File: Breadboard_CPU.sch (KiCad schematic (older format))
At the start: 21 parts, among them Q101 2N2222, SW101 RST

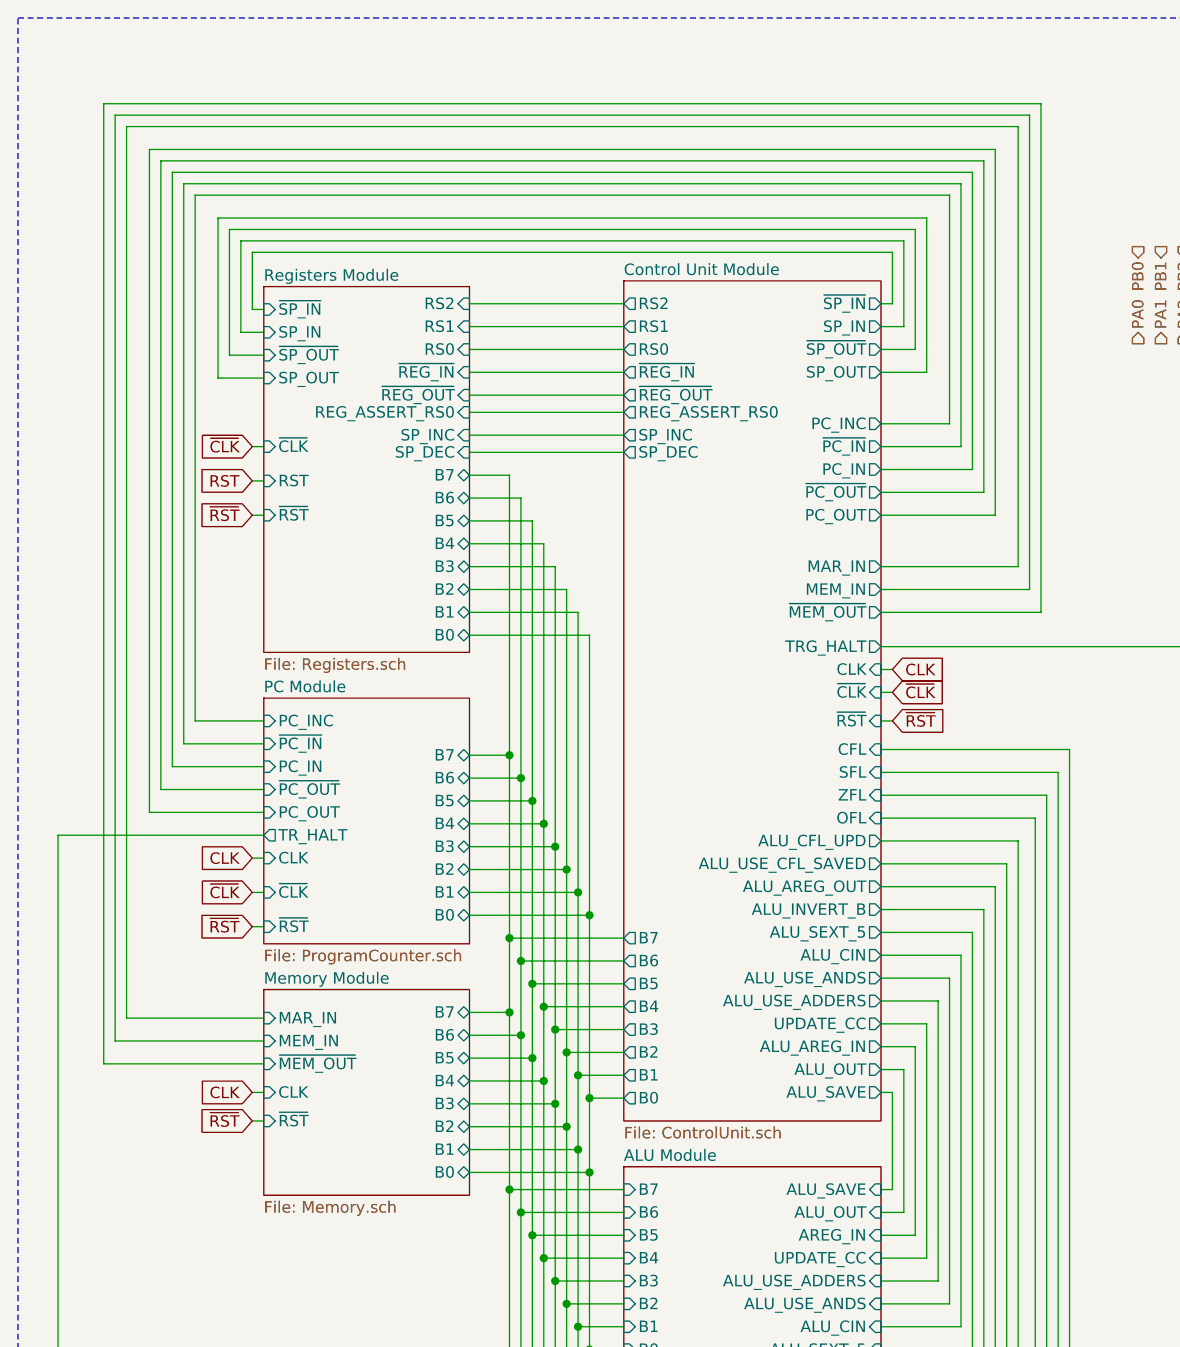
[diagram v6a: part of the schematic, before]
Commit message: Pre-removal of H/L byte deciding hardware
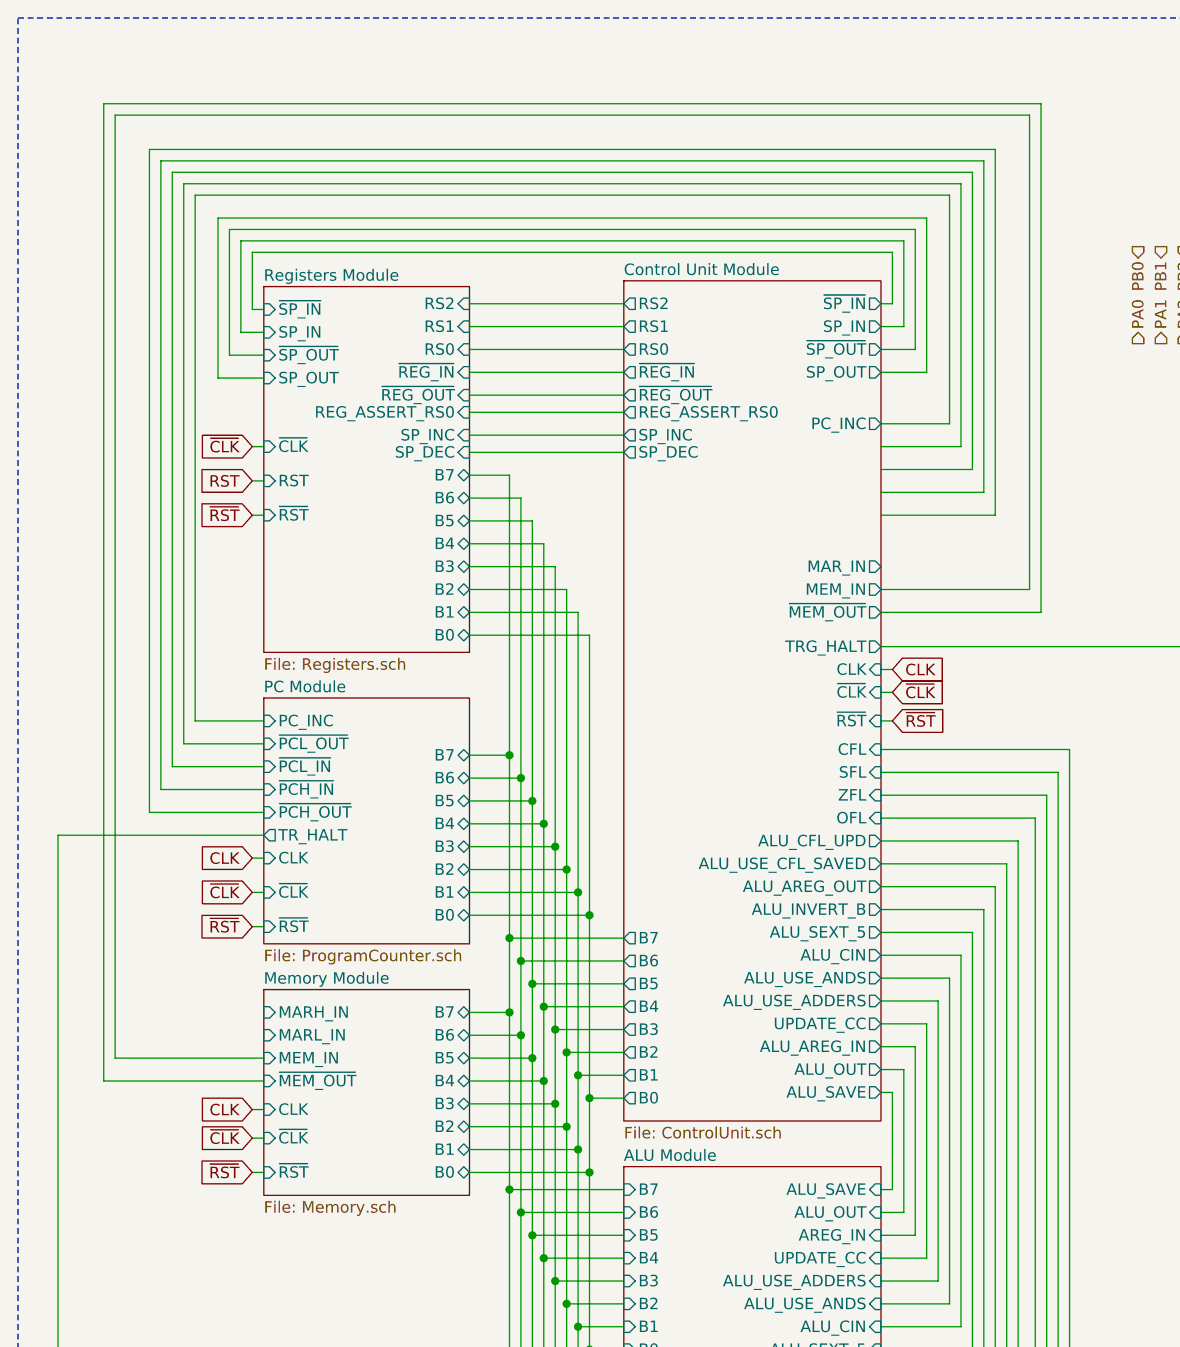
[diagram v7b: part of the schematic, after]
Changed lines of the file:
@@
 F8 "B6" B R 4200 6025 50
 F9 "B7" B R 4200 5925 50
-F10 "CLK" I L 3300 6275 50
-F11 "MAR_IN" I L 3300 5950 50
-F12 "~MEM_OUT" I L 3300 6150 50
-F13 "MEM_IN" I L 3300 6050 50
-F14 "~RST" I L 3300 6400 50
+F10 "CLK" I L 3300 6350 50
+F11 "~MEM_OUT" I L 3300 6225 50
+F12 "MEM_IN" I L 3300 6125 50
+F13 "~RST" I L 3300 6625 50
+F14 "~CLK" I L 3300 6475 50
+F15 "MARH_IN" I L 3300 5925 50
+F16 "MARL_IN" I L 3300 6025 50
 $EndSheet
 $Sheet
@@
 F24 "ZFL" I R 6000 4975 50
 F25 "SFL" I R 6000 4875 50
-F26 "~PC_OUT" O R 6000 3650 50
-F27 "~PC_IN" O R 6000 3450 50
-F28 "~MEM_OUT" O R 6000 4175 50
-F29 "SP_INC" O L 4875 3400 50
-F30 "SP_DEC" O L 4875 3475 50
-F31 "ALU_USE_ADDERS" O R 6000 5875 50
-F32 "ALU_USE_ANDS" O R 6000 5775 50
-F33 "ALU_CIN" O R 6000 5675 50
-F34 "ALU_SEXT_5" O R 6000 5575 50
-F35 "ALU_INVERT_B" O R 6000 5475 50
-F36 "ALU_USE_CFL_SAVED" O R 6000 5275 50
-F37 "PC_IN" O R 6000 3550 50
-F38 "PC_OUT" O R 6000 3750 50
-F39 "ALU_OUT" O R 6000 6175 50
-F40 "ALU_AREG_OUT" O R 6000 5375 50
-F41 "~SP_IN" O R 6000 2825 50
-F42 "~SP_OUT" O R 6000 3025 50
-F43 "SP_OUT" O R 6000 3125 50
-F44 "SP_IN" O R 6000 2925 50
-F45 "ALU_CFL_UPD" O R 6000 5175 50
-F46 "ALU_AREG_IN" O R 6000 6075 50
-F47 "TRG_HALT" O R 6000 4325 50
-F48 "CFL" I R 6000 4775 50
-F49 "REG_ASSERT_RS0" O L 4875 3300 50
+F26 "~MEM_OUT" O R 6000 4175 50
+F27 "SP_INC" O L 4875 3400 50
+F28 "SP_DEC" O L 4875 3475 50
+F29 "ALU_USE_ADDERS" O R 6000 5875 50
+F30 "ALU_USE_ANDS" O R 6000 5775 50
+F31 "ALU_CIN" O R 6000 5675 50
+F32 "ALU_SEXT_5" O R 6000 5575 50
+F33 "ALU_INVERT_B" O R 6000 5475 50
+F34 "ALU_USE_CFL_SAVED" O R 6000 5275 50
+F35 "ALU_OUT" O R 6000 6175 50
+F36 "ALU_AREG_OUT" O R 6000 5375 50
+F37 "~SP_IN" O R 6000 2825 50
+F38 "~SP_OUT" O R 6000 3025 50
+F39 "SP_OUT" O R 6000 3125 50
+F40 "SP_IN" O R 6000 2925 50
+F41 "ALU_CFL_UPD" O R 6000 5175 50
+F42 "ALU_AREG_IN" O R 6000 6075 50
+F43 "TRG_HALT" O R 6000 4325 50
+F44 "CFL" I R 6000 4775 50
+F45 "REG_ASSERT_RS0" O L 4875 3300 50
 $EndSheet
 Wire Wire Line
@@
 F10 "PC_INC" I L 3300 4650 50
 F11 "~RST" I L 3300 5550 50
-F12 "~PC_OUT" I L 3300 4950 50
-F13 "CLK" I L 3300 5250 50
-F14 "~PC_IN" I L 3300 4750 50
-F15 "TR_HALT" O L 3300 5150 50
-F16 "PC_IN" I L 3300 4850 50
-F17 "PC_OUT" I L 3300 5050 50
-F18 "~CLK" I L 3300 5400 50
+F12 "CLK" I L 3300 5250 50
+F13 "TR_HALT" O L 3300 5150 50
+F14 "~CLK" I L 3300 5400 50
+F15 "~PCL_OUT" I L 3300 4750 50
+F16 "~PCL_IN" I L 3300 4850 50
+F17 "~PCH_IN" I L 3300 4950 50
+F18 "~PCH_OUT" I L 3300 5050 50
 $EndSheet
 Wire Wire Line
@@
 	4725 6625 4725 7400
 Wire Wire Line
-	6000 3975 6600 3975
-Wire Wire Line
-	6600 3975 6600 2050
-Wire Wire Line
-	6600 2050 2700 2050
-Wire Wire Line
-	2700 2050 2700 5950
-Wire Wire Line
-	2700 5950 3300 5950
-Wire Wire Line
-	3300 6050 2650 6050
-Wire Wire Line
-	2650 6050 2650 2000
+	3300 6125 2650 6125
 Wire Wire Line
 	2650 2000 6650 2000
@@
 	6700 4175 6700 1950
 Wire Wire Line
-	6700 1950 2600 1950
-Wire Wire Line
-	2600 1950 2600 6150
-Wire Wire Line
-	2600 6150 3300 6150
+	2600 6225 3300 6225
 Text GLabel 6050 8475 2    50   Input ~ 0
 ~RST
@@
 Wire Wire Line
 	3300 5250 3250 5250
-Text GLabel 3250 6400 0    50   Input ~ 0
+Text GLabel 3250 6625 0    50   Input ~ 0
 ~RST
 Wire Wire Line
-	3300 6400 3250 6400
-Text GLabel 3250 6275 0    50   Input ~ 0
+	3300 6625 3250 6625
+Text GLabel 3250 6350 0    50   Input ~ 0
 CLK
 Wire Wire Line
-	3300 6275 3250 6275
+	3300 6350 3250 6350
 Text GLabel 6925 10025 2    50   Output ~ 0
 ~RST
@@
 Wire Wire Line
 	4200 3300 4875 3300
+Text GLabel 3250 6475 0    50   Input ~ 0
+~CLK
+Wire Wire Line
+	3250 6475 3300 6475
+Wire Wire Line
+	6700 1950 2600 1950
+Wire Wire Line
+	2600 1950 2600 6225
+Wire Wire Line
+	2650 6125 2650 2000
 $EndSCHEMATC
